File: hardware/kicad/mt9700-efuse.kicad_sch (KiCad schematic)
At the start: 9 parts, among them U67 MT9700-N, U68 150uF

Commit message: starting erc check
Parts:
- C78, C79, C80: footprint Capacitor_SMD:C_0603_1608Metric -> 5v rail sm-easyedapro:C0603
- R144, R145, R146: footprint Resistor_SMD:R_0603_1608Metric -> 5v rail sm-easyedapro:R0603
- U67: footprint Package_TO_SOT_SMD:SOT-23-5 -> 5v rail sm-easyedapro:SOT-23-5_L2.9-W1.6-P0.95-LS2.9-BL
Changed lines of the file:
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@@
 			)
 		)
-		(property "Description" ""
+		(property "Description" "Power symbol creates a global label with name \"GND\" , ground"
 			(at 160.02 102.87 0)
 			(effects
@@
 			)
 		)
-		(property "Footprint" "Resistor_SMD:R_0603_1608Metric"
+		(property "Footprint" "5v rail sm-easyedapro:R0603"
 			(at 109.22 97.79 0)
 			(effects
@@
 			)
 		)
-		(property "Footprint" "Capacitor_SMD:C_0603_1608Metric"
+		(property "Footprint" "5v rail sm-easyedapro:C0603"
 			(at 69.85 88.9 0)
 			(effects
@@
 			)
 		)
-		(property "Description" ""
+		(property "Description" "Power symbol creates a global label with name \"GND\" , ground"
 			(at 116.84 125.73 0)
 			(effects
@@
 			)
 		)
-		(property "Description" ""
+		(property "Description" "Power symbol creates a global label with name \"GND\" , ground"
 			(at 78.74 105.41 0)
 			(effects
@@
 			)
 		)
-		(property "Datasheet" ""
+		(property "Datasheet" "~"
 			(at 116.84 120.65 0)
 			(effects
@@
 			)
 		)
-		(property "Description" ""
+		(property "Description" "Jumper, 2-pole, open"
 			(at 116.84 120.65 0)
 			(effects
@@
 			)
 		)
-		(property "Footprint" "Capacitor_SMD:C_0603_1608Metric"
+		(property "Footprint" "5v rail sm-easyedapro:C0603"
 			(at 194.31 88.9 0)
 			(effects
@@
 			)
 		)
-		(property "Footprint" "Resistor_SMD:R_0603_1608Metric"
+		(property "Footprint" "5v rail sm-easyedapro:R0603"
 			(at 116.84 110.49 0)
 			(effects
@@
 			)
 		)
-		(property "Footprint" "Resistor_SMD:R_0603_1608Metric"
+		(property "Footprint" "5v rail sm-easyedapro:R0603"
 			(at 116.84 83.82 0)
 			(effects
@@
 			)
 		)
-		(property "Footprint" "Package_TO_SOT_SMD:SOT-23-5"
+		(property "Footprint" "5v rail sm-easyedapro:SOT-23-5_L2.9-W1.6-P0.95-LS2.9-BL"
 			(at 143.51 78.74 0)
 			(effects
@@
 			)
 		)
-		(property "Footprint" "Capacitor_SMD:C_0603_1608Metric"
+		(property "Footprint" "5v rail sm-easyedapro:C0603"
 			(at 86.36 88.9 0)
 			(effects

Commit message: various improvements
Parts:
- removed R144: 47Ω, 5v rail sm-easyedapro:R0603, symbol 5v rail sm-easyedapro:RS-03K47R0FT
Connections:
- net EN: now also R145.1, R146.2, U67.4 (EN)
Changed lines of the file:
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@@
-	(wire
-		(pts
-			(xy 114.3 97.79) (xy 116.84 97.79)
-		)
-		(stroke
-			(width 0)
-			(type default)
-		)
-	)
 	(wire
 		(pts
@@
 		(pts
 			(xy 129.54 97.79) (xy 129.54 81.28)
+		)
+		(stroke
+			(width 0)
+			(type default)
+		)
+	)
+	(wire
+		(pts
+			(xy 104.14 97.79) (xy 116.84 97.79)
 		)
 		(stroke
@@
 					(unit 1)
 				)
-			)
-		)
-	)
-	(symbol
-		(lib_id "5v rail sm-easyedapro:RS-03K47R0FT")
-		(at 109.22 97.79 0)
-		(unit 1)
-		(exclude_from_sim no)
-		(in_bom yes)
-		(on_board yes)
-		(dnp no)
-		(property "Reference" "R144"
-			(at 106.68 101.6 0)
-			(effects
-				(font
-					(size 1.27 1.27)
-				)
-				(justify left bottom)
-			)
-		)
-		(property "Value" "47Ω"
-			(at 106.68 104.14 0)
-			(effects
-				(font
-					(size 1.27 1.27)
-				)
-				(justify left bottom)
-			)
-		)
-		(property "Footprint" "5v rail sm-easyedapro:R0603"
-			(at 109.22 97.79 0)
-			(effects
-				(font
-					(size 1.27 1.27)
-				)
-				(hide yes)
-			)
-		)
-		(property "Datasheet" "https://atta.szlcsc.com/upload/public/pdf/source/20140616/1457707091974.pdf"
-			(at 109.22 97.79 0)
-			(effects
-				(font
-					(size 1.27 1.27)
-				)
-				(hide yes)
-			)
-		)
-		(property "Description" "Type:Thick Film Resistors Resistance: Tolerance:±1% Tolerance:±1% Power(Watts): Overload Voltage (Max): Temperature Coefficient:±100ppm/°C Temperature Coefficient:±100ppm/°C Operating Temperature Range:-55°C~+155°C Operating Temperature Range:-55°C~+155°C"
-			(at 109.22 97.79 0)
-			(effects
-				(font
-					(size 1.27 1.27)
-				)
-				(hide yes)
-			)
-		)
-		(property "Manufacturer Part" "RS-03K47R0FT"
-			(at 109.22 97.79 0)
-			(effects
-				(font
-					(size 1.27 1.27)
-				)
-				(hide yes)
-			)
-		)
-		(property "Manufacturer" "FH(风华)"
-			(at 109.22 97.79 0)
-			(effects
-				(font
-					(size 1.27 1.27)
-				)
-				(hide yes)
-			)
-		)
-		(property "Supplier Part" "C140087"
-			(at 109.22 97.79 0)
-			(effects
-				(font
-					(size 1.27 1.27)
-				)
-				(hide yes)
-			)
-		)
-		(property "Supplier" "LCSC"
-			(at 109.22 97.79 0)
-			(effects
-				(font
-					(size 1.27 1.27)
-				)
-				(hide yes)
-			)
-		)
-		(property "LCSC Part Name" "厚膜电阻 47Ω ±1% 100mW"
-			(at 109.22 97.79 0)
-			(effects
-				(font
-					(size 1.27 1.27)
-				)
-				(hide yes)
-			)
-		)
-		(pin "1"
-		)
-		(pin "2"
-		)
-		(instances
-			(project "svea_powerboard_rev3"
-				(path "/3f85abf4-0b95-4c4a-b7e9-06f59ca1ea3d/5c2e021f-c2d4-49e2-8c36-9a64f1f12001/1d4a251e-4375-4aab-85e0-d11dfb5595c0"
-					(reference "R144")
-					(unit 1)
-				)
-				(path "/3f85abf4-0b95-4c4a-b7e9-06f59ca1ea3d/5c2e021f-c2d4-49e2-8c36-9a64f1f12001/a553934f-48fa-4d71-a435-79ebd566d680"
-					(reference "R167")
-					(unit 1)
-				)

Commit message: update
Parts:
- removed R146: 4.7kΩ, 5v rail sm-easyedapro:R0603, symbol 5v rail sm-easyedapro:0603WAF4701T5E
- removed U66: ~, Jumper:SolderJumper-2_P1.3mm_Open_Pad1.0x1.5mm, symbol Jumper:Jumper_2_Open

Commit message: update
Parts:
- removed U68: 150uF, 5v rail sm-easyedapro:CAP-SMD_BD6.3-L6.6-W6.6-LS7.4-FD, symbol 5v rail sm-easyedapro:RVT1V151M0607
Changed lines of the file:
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@@
-	)
-	(symbol
-		(lib_id "5v rail sm-easyedapro:RVT1V151M0607")
-		(at 180.34 88.9 270)
-		(unit 1)
-		(exclude_from_sim no)
-		(in_bom yes)
-		(on_board yes)
-		(dnp no)
-		(property "Reference" "U68"
-			(at 184.15 88.9 90)
-			(effects
-				(font
-					(size 1.27 1.27)
-				)
-				(justify left bottom)
-			)
-		)
-		(property "Value" "150uF"
-			(at 184.15 91.44 90)
-			(effects
-				(font
-					(size 1.27 1.27)
-				)
-				(justify left bottom)
-			)
-		)
-		(property "Footprint" "5v rail sm-easyedapro:CAP-SMD_BD6.3-L6.6-W6.6-LS7.4-FD"
-			(at 180.34 88.9 0)
-			(effects
-				(font
-					(size 1.27 1.27)
-				)
-				(hide yes)
-			)
-		)
-		(property "Datasheet" ""
-			(at 180.34 88.9 0)
-			(effects
-				(font
-					(size 1.27 1.27)
-				)
-				(hide yes)
-			)
-		)
-		(property "Description" "Capacitance:150uF Tolerance:±20% Tolerance:±20% Voltage Rating:35V Ripple Current:118mA@120Hz Diameter:6.3mm Height - Seated (Max):7.7mm Lifetime:2000hrs@105°C Operating Temperature:-40°C~+105°C Operating Temperature:-40°C~+105°C"
-			(at 180.34 88.9 0)
-			(effects
-				(font
-					(size 1.27 1.27)
-				)
-				(hide yes)
-			)
-		)
-		(property "Manufacturer Part" "RVT1V151M0607"
-			(at 180.34 88.9 0)
-			(effects
-				(font
-					(size 1.27 1.27)
-				)
-				(hide yes)
-			)
-		)
-		(property "Manufacturer" "ROQANG(容强)"
-			(at 180.34 88.9 0)
-			(effects
-				(font
-					(size 1.27 1.27)
-				)
-				(hide yes)
-			)
-		)
-		(property "Supplier Part" "C3032176"
-			(at 180.34 88.9 0)
-			(effects
-				(font
-					(size 1.27 1.27)
-				)
-				(hide yes)
-			)
-		)
-		(property "Supplier" "LCSC"
-			(at 180.34 88.9 0)
-			(effects
-				(font
-					(size 1.27 1.27)
-				)
-				(hide yes)
-			)
-		)
-		(property "LCSC Part Name" "150uF ±20% 35V"
-			(at 180.34 88.9 0)
-			(effects
-				(font
-					(size 1.27 1.27)
-				)
-				(hide yes)
-			)
-		)
-		(pin "1"
-		)
-		(pin "2"
-		)
-		(instances
-			(project "svea_powerboard_rev3"
-				(path "/3f85abf4-0b95-4c4a-b7e9-06f59ca1ea3d/5c2e021f-c2d4-49e2-8c36-9a64f1f12001/1d4a251e-4375-4aab-85e0-d11dfb5595c0"
-					(reference "U68")
-					(unit 1)
-				)
-				(path "/3f85abf4-0b95-4c4a-b7e9-06f59ca1ea3d/5c2e021f-c2d4-49e2-8c36-9a64f1f12001/a553934f-48fa-4d71-a435-79ebd566d680"
-					(reference "U77")
-					(unit 1)
-				)
-			)
-		)
 	)
 	(symbol

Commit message: updating symbols to use kicad footprints where possible
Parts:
- C78, C79, C80: footprint 5v rail sm-easyedapro:C0603 -> Capacitor_SMD:C_0603_1608Metric
- R145: footprint 5v rail sm-easyedapro:R0603 -> Resistor_SMD:R_0603_1608Metric
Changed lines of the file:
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@@
 			)
 		)
-		(property "Footprint" "5v rail sm-easyedapro:C0603"
+		(property "Footprint" "Capacitor_SMD:C_0603_1608Metric"
 			(at 69.85 88.9 0)
 			(effects
@@
 			)
 		)
-		(property "Footprint" "5v rail sm-easyedapro:C0603"
+		(property "Footprint" "Capacitor_SMD:C_0603_1608Metric"
 			(at 194.31 88.9 0)
 			(effects
@@
 			)
 		)
-		(property "Footprint" "5v rail sm-easyedapro:R0603"
+		(property "Footprint" "Resistor_SMD:R_0603_1608Metric"
 			(at 116.84 83.82 0)
 			(effects
@@
 			)
 		)
-		(property "Footprint" "5v rail sm-easyedapro:C0603"
+		(property "Footprint" "Capacitor_SMD:C_0603_1608Metric"
 			(at 86.36 88.9 0)
 			(effects

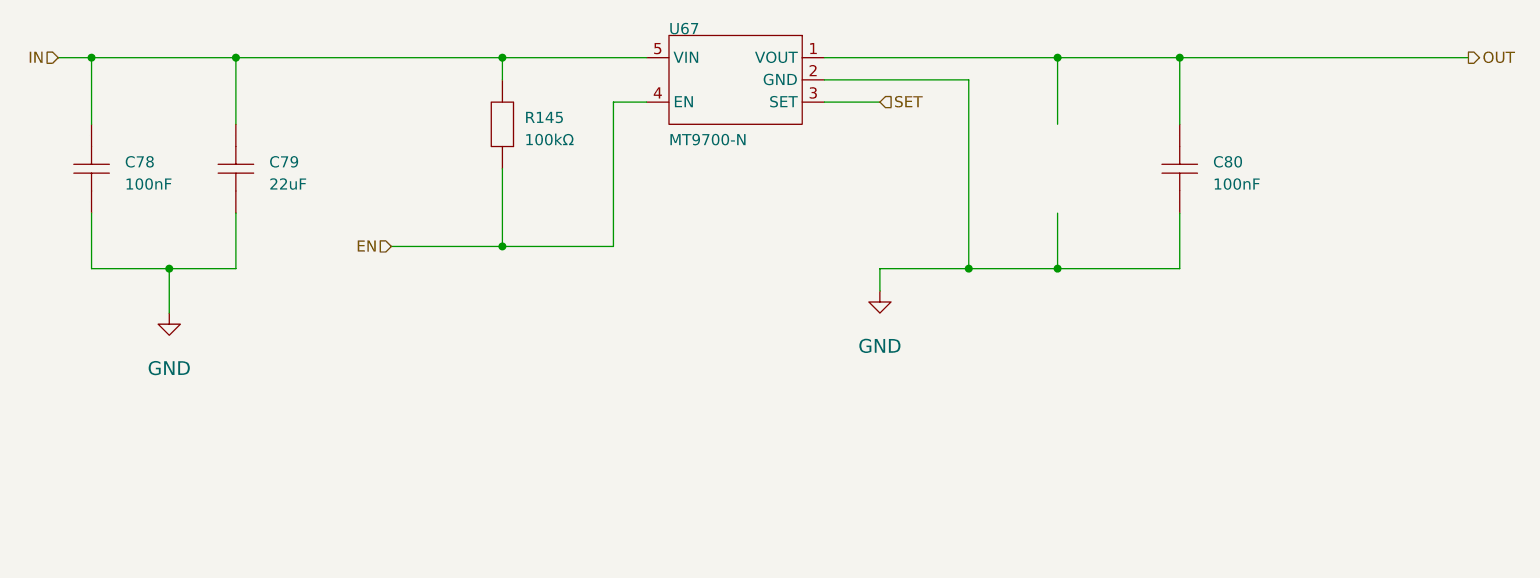
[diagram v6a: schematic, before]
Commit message: fixing inconsistencies in value convention
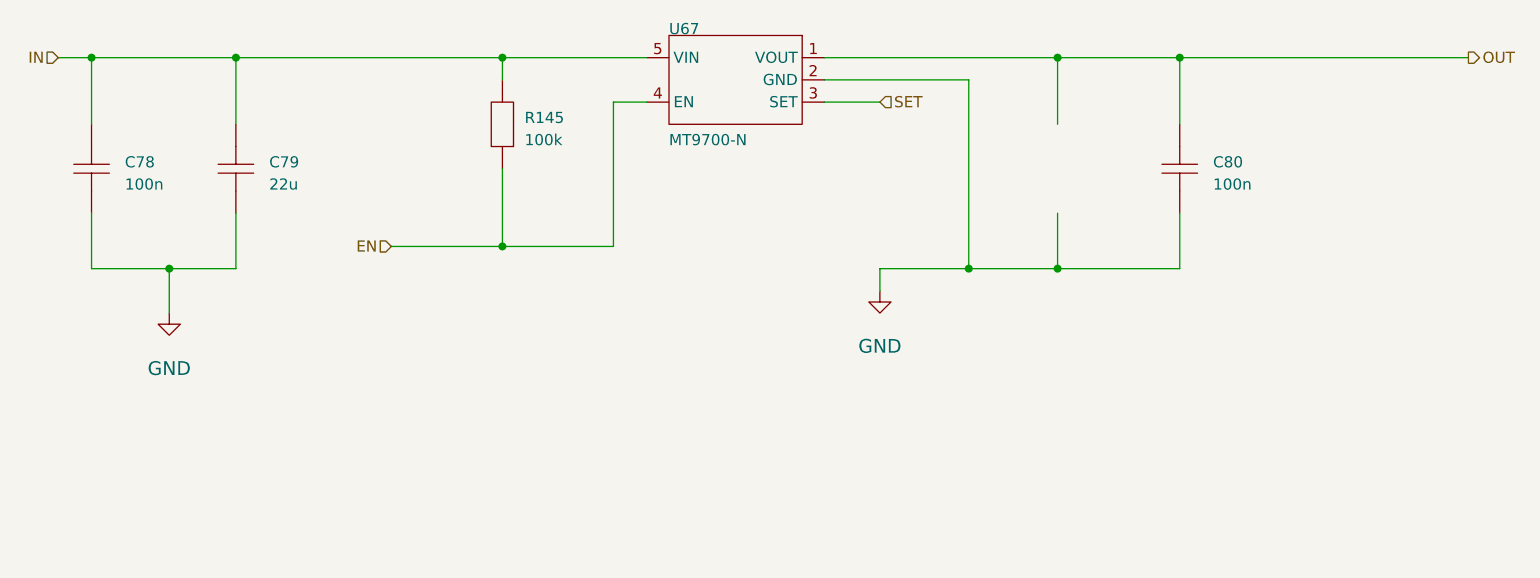
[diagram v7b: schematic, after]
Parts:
- C78, C80: value 100nF -> 100n
- C79: value 22uF -> 22u
- R145: value 100kΩ -> 100k
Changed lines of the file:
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@@
 			)
 		)
-		(property "Value" "100nF"
+		(property "Value" "100n"
 			(at 73.66 91.44 90)
 			(effects
@@
 			)
 		)
-		(property "Value" "100nF"
+		(property "Value" "100n"
 			(at 198.12 91.44 90)
 			(effects
@@
 			)
 		)
-		(property "Value" "100kΩ"
+		(property "Value" "100k"
 			(at 119.38 86.36 90)
 			(effects
@@
 			)
 		)
-		(property "Value" "22uF"
+		(property "Value" "22u"
 			(at 90.17 91.44 90)
 			(effects

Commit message: exported to schematic
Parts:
- C78, C80: LCSC (none) -> C14663
- C79: LCSC (none) -> C86295
- R145: LCSC (none) -> C25803
- U67: LCSC (none) -> C42441843
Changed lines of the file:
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@@
+			)
+		)
+		(property "LCSC" "C14663"
+			(at 73.66 88.9 0)
+			(effects
+				(font
+					(size 1.27 1.27)
+				)
+				(hide yes)
 			)
 		)
@@
 			)
 		)
+		(property "LCSC" "C14663"
+			(at 198.12 88.9 0)
+			(effects
+				(font
+					(size 1.27 1.27)
+				)
+				(hide yes)
+			)
+		)
 		(pin "1"
 		)
@@
 		(property "LCSC Part Name" "100kΩ ±5% 100mW 厚膜电阻"
 			(at 116.84 83.82 0)
+			(effects
+				(font
+					(size 1.27 1.27)
+				)
+				(hide yes)
+			)
+		)
+		(property "LCSC" "C25803"
+			(at 119.38 83.82 0)
 			(effects
 				(font
@@
 			)
 		)
+		(property "LCSC" "C42441843"
+			(at 135.89 73.66 0)
+			(effects
+				(font
+					(size 1.27 1.27)
+				)
+				(hide yes)
+			)
+		)
 		(pin "3"
 		)
@@
 			(effects
 				(font
+					(size 1.27 1.27)
+				)
+				(hide yes)
+			)
+		)
+		(property "LCSC" "C86295"
+			(at 90.17 88.9 0)
+			(effects
+				(font
